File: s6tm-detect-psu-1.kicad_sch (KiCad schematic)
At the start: 73 parts, among them J1 Conn_01x02, J2 Conn_01x02, J3 USB_C_Receptacle_USB2.0_14P, U1 TPS259470x, U2 TPS259470x, U3 TPS259470x, U4 TPS62933, U5 TPS259470x

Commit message: schem: update some 10u footprints
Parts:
- C10, C7, C8, C9: footprint Capacitor_SMD:C_0402_1005Metric -> Capacitor_SMD:C_0805_2012Metric; JLCPCB Part # C15525 -> C440198; Manufacturer Samsung Electro-Mechanics -> Murata; Manufacturer Part Number CL05A106MQ5NUNC -> GRM21BR61H106KE43L
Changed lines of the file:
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@@
 			)
 		)
-		(property "Footprint" "Capacitor_SMD:C_0402_1005Metric"
+		(property "Footprint" "Capacitor_SMD:C_0805_2012Metric"
 			(at 104.4448 97.79 0)
 			(hide yes)
@@
 			)
 		)
-		(property "JLCPCB Part #" "C15525"
+		(property "JLCPCB Part #" "C440198"
 			(at 105.41 93.98 0)
 			(hide yes)
@@
 			)
 		)
-		(property "Manufacturer" "Samsung Electro-Mechanics "
+		(property "Manufacturer" "Murata"
 			(at 105.41 93.98 0)
 			(hide yes)
@@
 			)
 		)
-		(property "Manufacturer Part Number" "CL05A106MQ5NUNC"
+		(property "Manufacturer Part Number" "GRM21BR61H106KE43L"
 			(at 105.41 93.98 0)
 			(hide yes)
@@
 			)
 		)
-		(property "Footprint" "Capacitor_SMD:C_0402_1005Metric"
+		(property "Footprint" "Capacitor_SMD:C_0805_2012Metric"
 			(at 111.4552 44.45 0)
 			(hide yes)
@@
 			)
 		)
-		(property "JLCPCB Part #" "C15525"
+		(property "JLCPCB Part #" "C440198"
 			(at 110.49 40.64 0)
 			(hide yes)
@@
 			)
 		)
-		(property "Manufacturer" "Samsung Electro-Mechanics "
+		(property "Manufacturer" "Murata"
 			(at 110.49 40.64 0)
 			(hide yes)
@@
 			)
 		)
-		(property "Manufacturer Part Number" "CL05A106MQ5NUNC"
+		(property "Manufacturer Part Number" "GRM21BR61H106KE43L"
 			(at 110.49 40.64 0)
 			(hide yes)
@@
 			)
 		)
-		(property "Footprint" "Capacitor_SMD:C_0402_1005Metric"
+		(property "Footprint" "Capacitor_SMD:C_0805_2012Metric"
 			(at 104.4448 44.45 0)
 			(hide yes)
@@
 			)
 		)
-		(property "JLCPCB Part #" "C15525"
+		(property "JLCPCB Part #" "C440198"
 			(at 105.41 40.64 0)
 			(hide yes)
@@
 			)
 		)
-		(property "Manufacturer" "Samsung Electro-Mechanics "
+		(property "Manufacturer" "Murata"
 			(at 105.41 40.64 0)
 			(hide yes)
@@
 			)
 		)
-		(property "Manufacturer Part Number" "CL05A106MQ5NUNC"
+		(property "Manufacturer Part Number" "GRM21BR61H106KE43L"
 			(at 105.41 40.64 0)
 			(hide yes)
@@
 			)
 		)
-		(property "Footprint" "Capacitor_SMD:C_0402_1005Metric"
+		(property "Footprint" "Capacitor_SMD:C_0805_2012Metric"
 			(at 111.4552 97.79 0)
 			(hide yes)
@@
 			)
 		)
-		(property "JLCPCB Part #" "C15525"
+		(property "JLCPCB Part #" "C440198"
 			(at 110.49 93.98 0)
 			(hide yes)
@@
 			)
 		)
-		(property "Manufacturer" "Samsung Electro-Mechanics "
+		(property "Manufacturer" "Murata"
 			(at 110.49 93.98 0)
 			(hide yes)
@@
 			)
 		)
-		(property "Manufacturer Part Number" "CL05A106MQ5NUNC"
+		(property "Manufacturer Part Number" "GRM21BR61H106KE43L"
 			(at 110.49 93.98 0)
 			(hide yes)

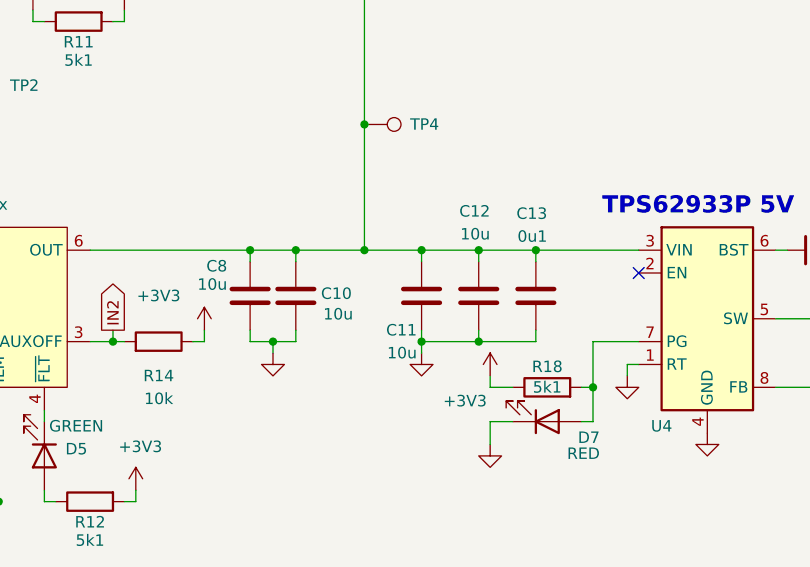
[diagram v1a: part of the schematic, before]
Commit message: pcb: add smps layout
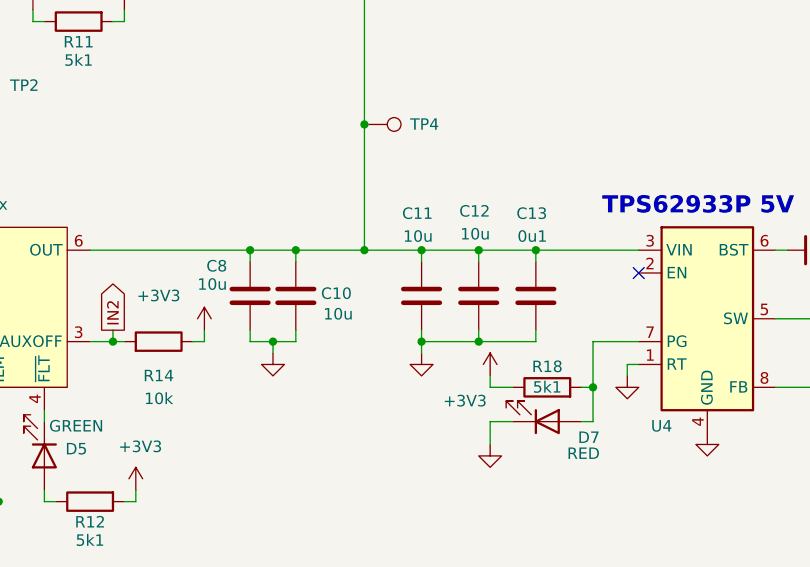
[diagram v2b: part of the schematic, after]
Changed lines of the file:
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@@
 		(dnp no)
 		(property "Reference" "C11"
-			(at 123.952 97.79 0)
+			(at 125.73 84.836 0)
 			(show_name no)
 			(do_not_autoplace no)
@@
 		)
 		(property "Value" "10u"
-			(at 123.952 100.33 0)
+			(at 125.73 87.376 0)
 			(show_name no)
 			(do_not_autoplace no)

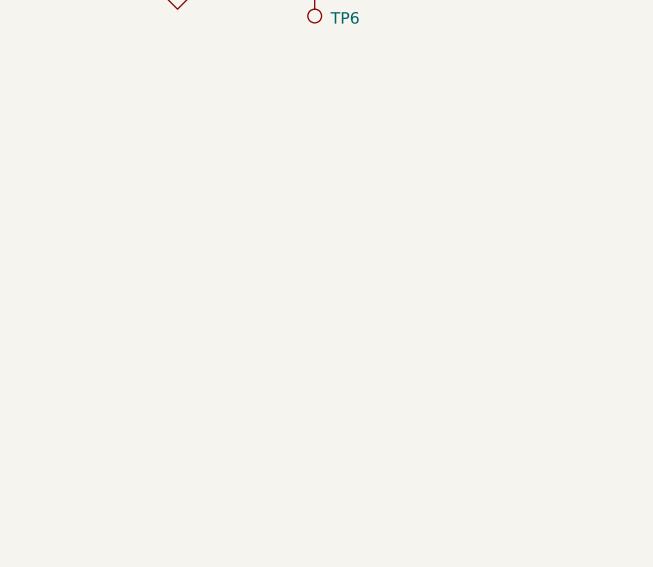
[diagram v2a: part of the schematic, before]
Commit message: schem/pcb: add mouting and tooling holes
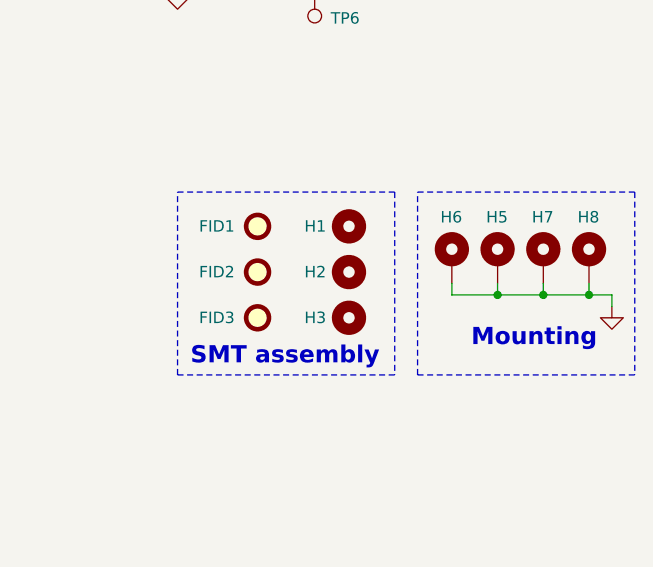
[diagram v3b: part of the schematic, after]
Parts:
- added FID1, FID2, FID3: Fiducial, Fiducial:Fiducial_1mm_Mask2mm, symbol Mechanical:Fiducial
- added H1, H2, H3: MountingHole, MountingHole:ToolingHole_1.152mm, symbol Mechanical:MountingHole
- added H5, H6, H7, H8: MountingHole_Pad, MountingHole:MountingHole_3.2mm_M3_Pad_Via, symbol Mechanical:MountingHole_Pad
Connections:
- net GND: now also H5.1, H6.1, H7.1, H8.1
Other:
- note added: "Mounting"
- note added: "SMT assembly"

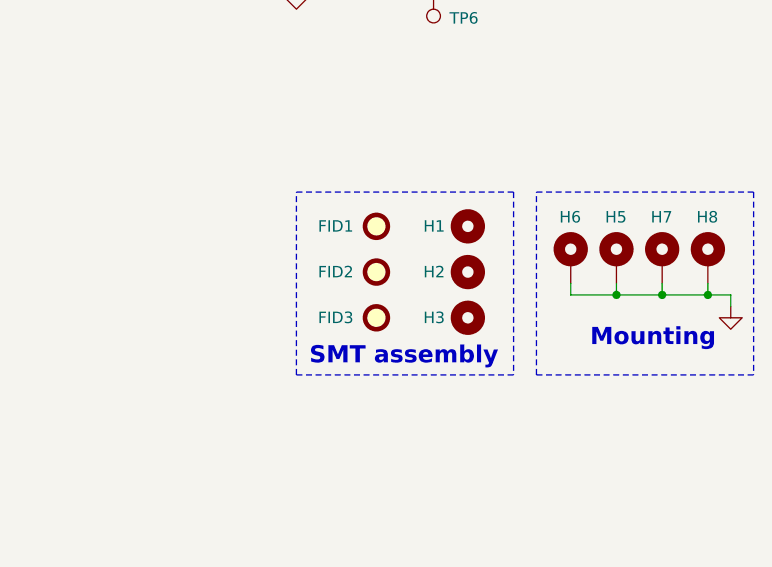
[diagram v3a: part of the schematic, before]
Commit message: schem: remove fiducials
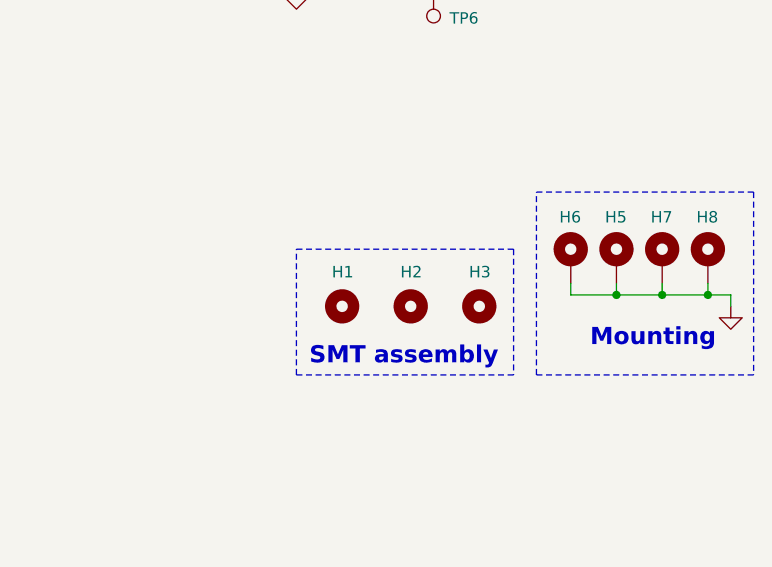
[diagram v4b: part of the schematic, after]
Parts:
- removed FID1, FID2, FID3: Fiducial, Fiducial:Fiducial_1mm_Mask2mm, symbol Mechanical:Fiducial
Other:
- moved on the sheet: H1, H2, H3

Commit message: pcb: finish board layout
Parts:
- removed H5: MountingHole_Pad, MountingHole:MountingHole_3.2mm_M3_Pad_Via, symbol Mechanical:MountingHole_Pad
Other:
- moved on the sheet: H1, H2, H3, H6, H7, H8

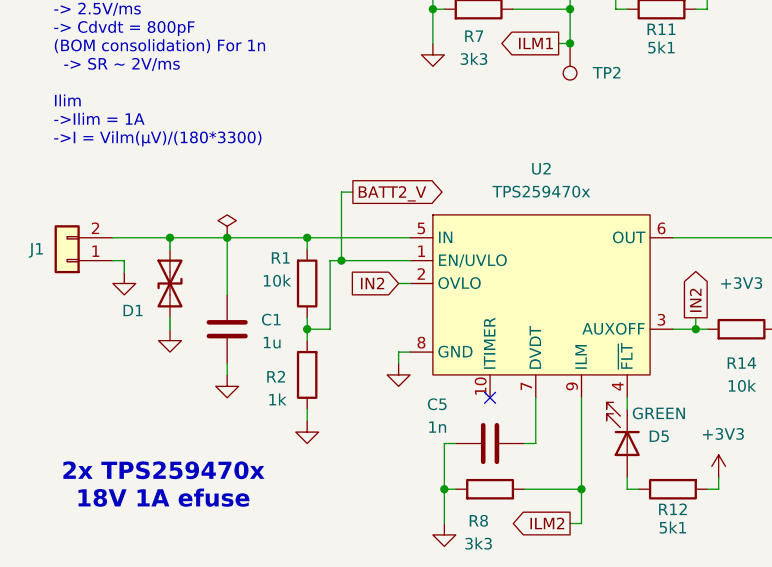
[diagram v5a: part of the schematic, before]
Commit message: pcb: add batt efuses routing
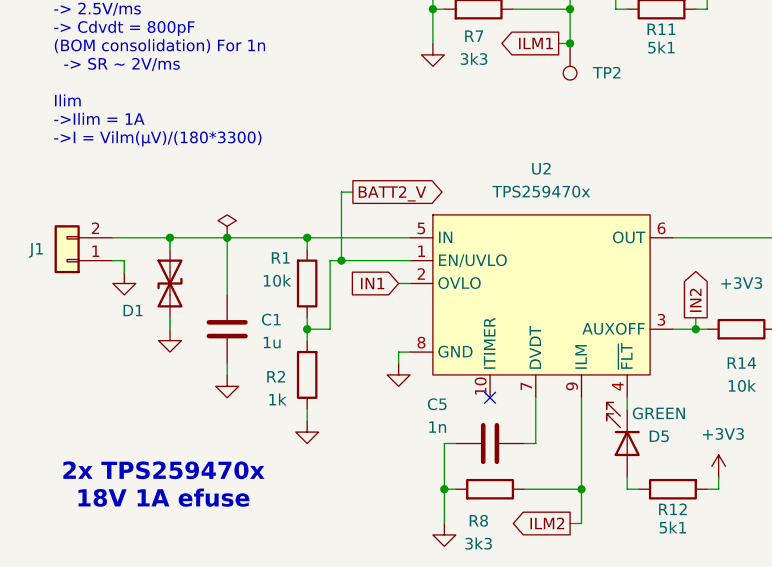
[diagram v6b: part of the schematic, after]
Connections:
- net IN1: now also U2.2 (OVLO)
- net IN2: no longer U2.2 (OVLO)
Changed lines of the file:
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@@
 		)
 	)
-	(global_label "IN2"
+	(global_label "IN1"
 		(shape input)
 		(at 57.15 93.98 180)

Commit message: schem: update resistor part number
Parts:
- R19: JLCPCB Part # C26982 -> C2998086; Manufacturer Uniroyal Elec -> FOJAN; Manufacturer Part Number 0402WGF5232TCE -> FRC0402F5232TS
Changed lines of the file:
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@@
 			)
 		)
-		(property "JLCPCB Part #" "C26982"
+		(property "JLCPCB Part #" "C2998086"
 			(at 181.61 93.98 90)
 			(hide yes)
@@
 			)
 		)
-		(property "Manufacturer" "Uniroyal Elec"
+		(property "Manufacturer" "FOJAN"
 			(at 181.61 93.98 90)
 			(hide yes)
@@
 			)
 		)
-		(property "Manufacturer Part Number" "0402WGF5232TCE"
+		(property "Manufacturer Part Number" "FRC0402F5232TS"
 			(at 181.61 93.98 90)
 			(hide yes)
